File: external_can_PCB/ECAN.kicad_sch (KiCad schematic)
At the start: 32 parts, among them J1 JST GH 4, J3 JST GH 6, J4 Micro_SD_Card, J5 JST GH 6, U1 SN65HVD232, U2 AP2127N-3.3, U5 STM32L562RETx, Y1 8 Mhz

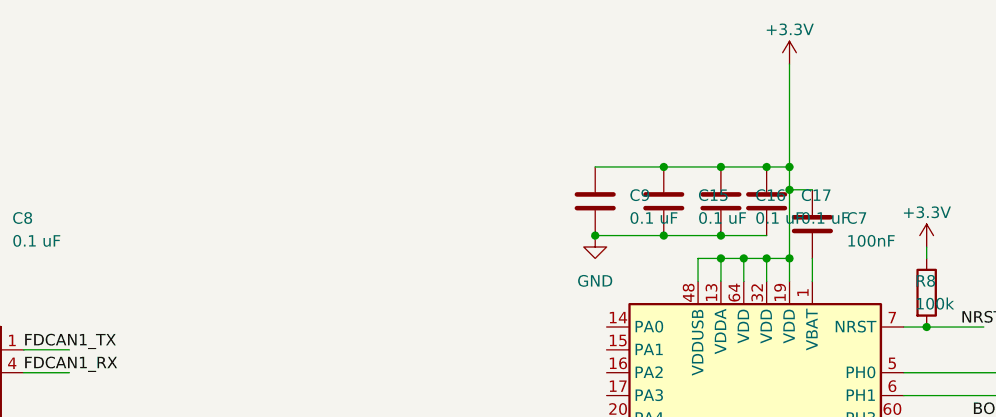
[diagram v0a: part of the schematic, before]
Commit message: Added screw holes and layer pours
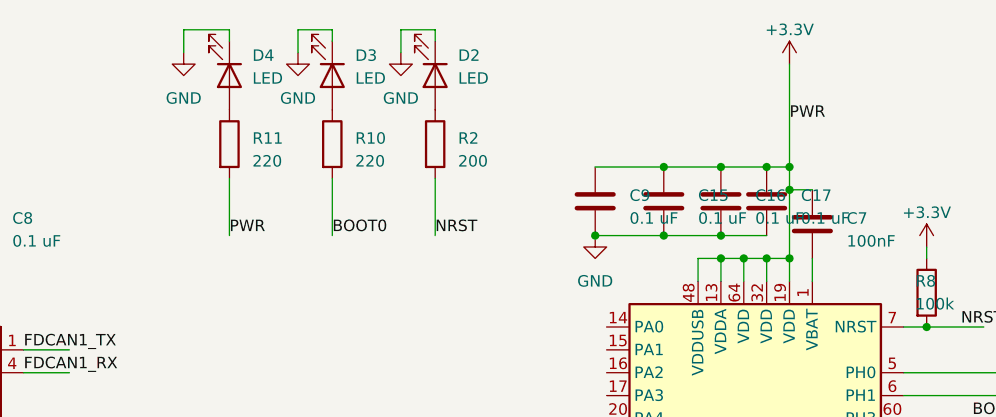
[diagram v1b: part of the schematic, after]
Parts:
- added D2, D3, D4: LED, LED_SMD:LED_0805_2012Metric_Pad1.15x1.40mm_HandSolder, symbol Device:LED
- added R10, R11: 220, Resistor_SMD:R_0402_1005Metric_Pad0.72x0.64mm_HandSolder, symbol Device:R
- added R2: 200, Resistor_SMD:R_0402_1005Metric_Pad0.72x0.64mm_HandSolder, symbol Device:R
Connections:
- net +3.3V: now also R11.2
- net BOOT0: now also R10.2
- net GND: now also D2.1 (K), D3.1 (K), D4.1 (K)
- net NRST: now also R2.2
- new net: D2.2 (A), R2.1
- new net: D4.2 (A), R11.1
- new net: D3.2 (A), R10.1

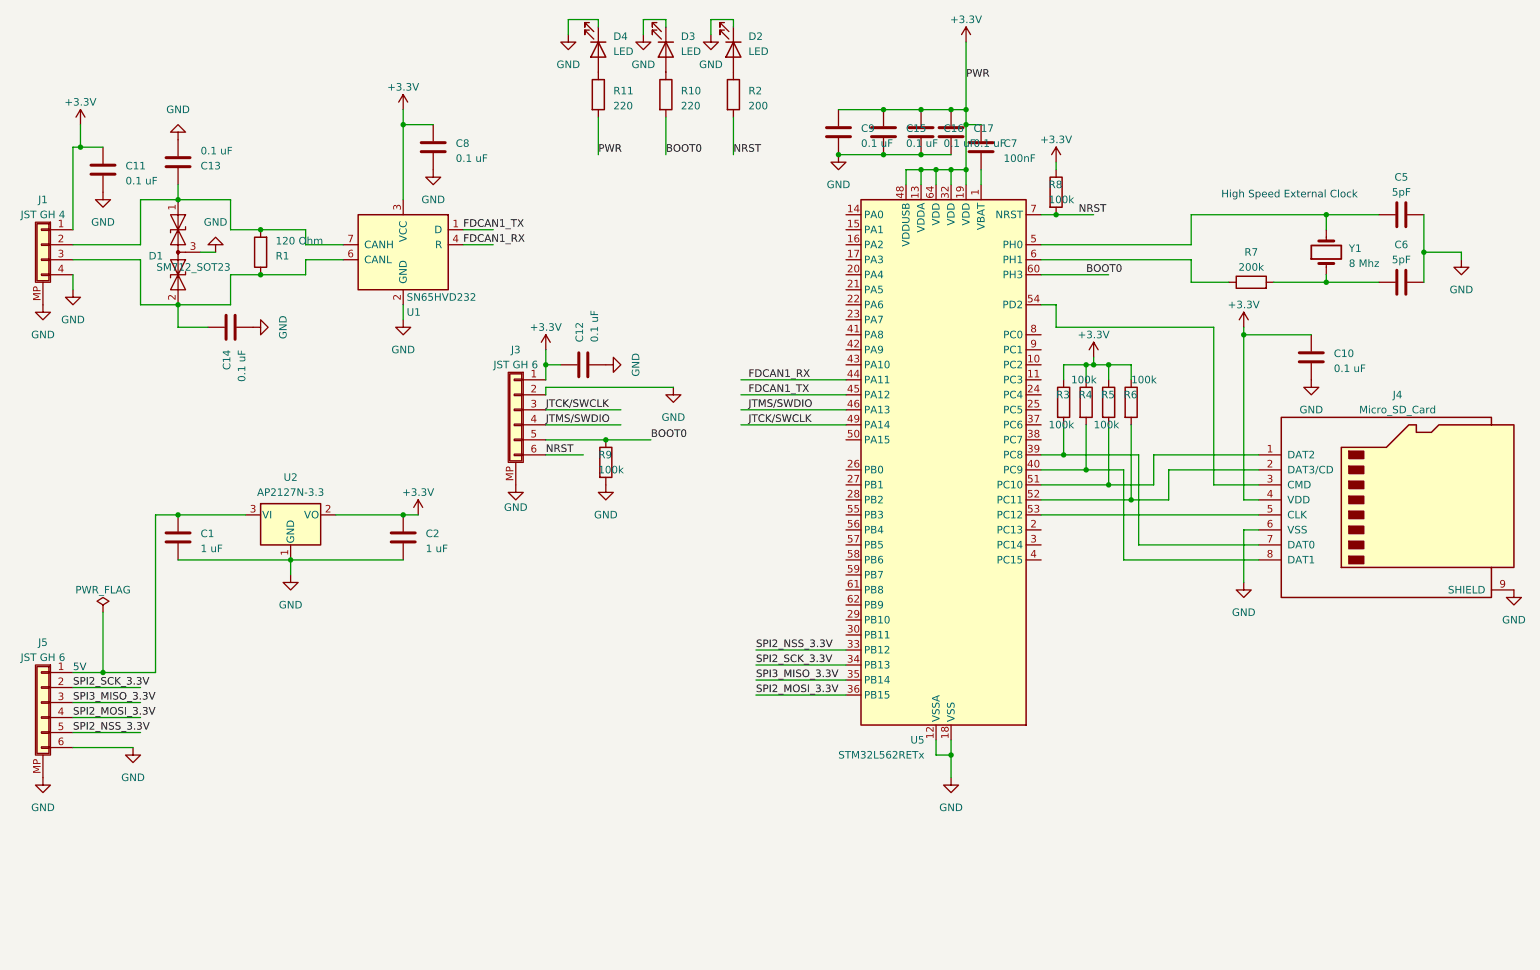
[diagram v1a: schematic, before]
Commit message: Addressed issues from Review by Olof
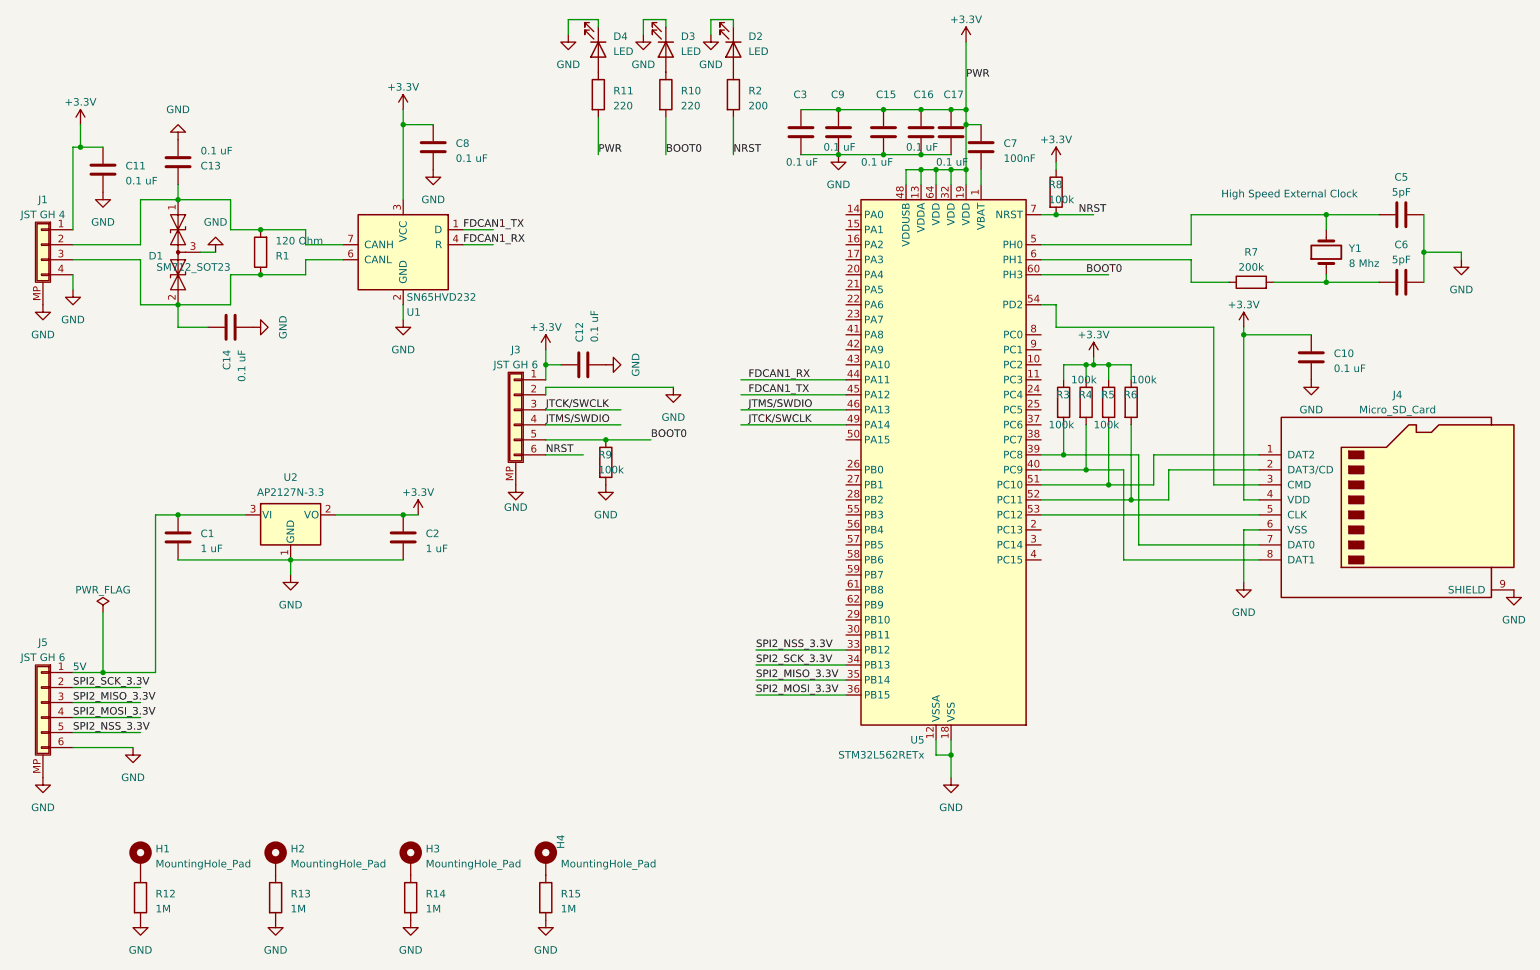
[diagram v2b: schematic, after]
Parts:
- added C3: 0.1 uF, Capacitor_SMD:C_0402_1005Metric_Pad0.74x0.62mm_HandSolder, symbol Device:C
- added H1, H2, H3, H4: MountingHole_Pad, MountingHole:MountingHole_3.2mm_M3_DIN965_Pad, symbol Mechanical:MountingHole_Pad
- added R12, R13, R14, R15: 1M, Resistor_SMD:R_0603_1608Metric_Pad0.98x0.95mm_HandSolder, symbol Device:R
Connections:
- net +3.3V: now also C3.1
- net GND: now also C3.2, R12.2, R13.2, R14.2, R15.2
- net SPI3_MISO_3.3V renamed SPI2_MISO_3.3V
- new net: H3.1, R14.1
- new net: H4.1, R15.1
- new net: H1.1, R12.1
- new net: H2.1, R13.1

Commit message: GPIO LED changes and UART connection to SPI lines
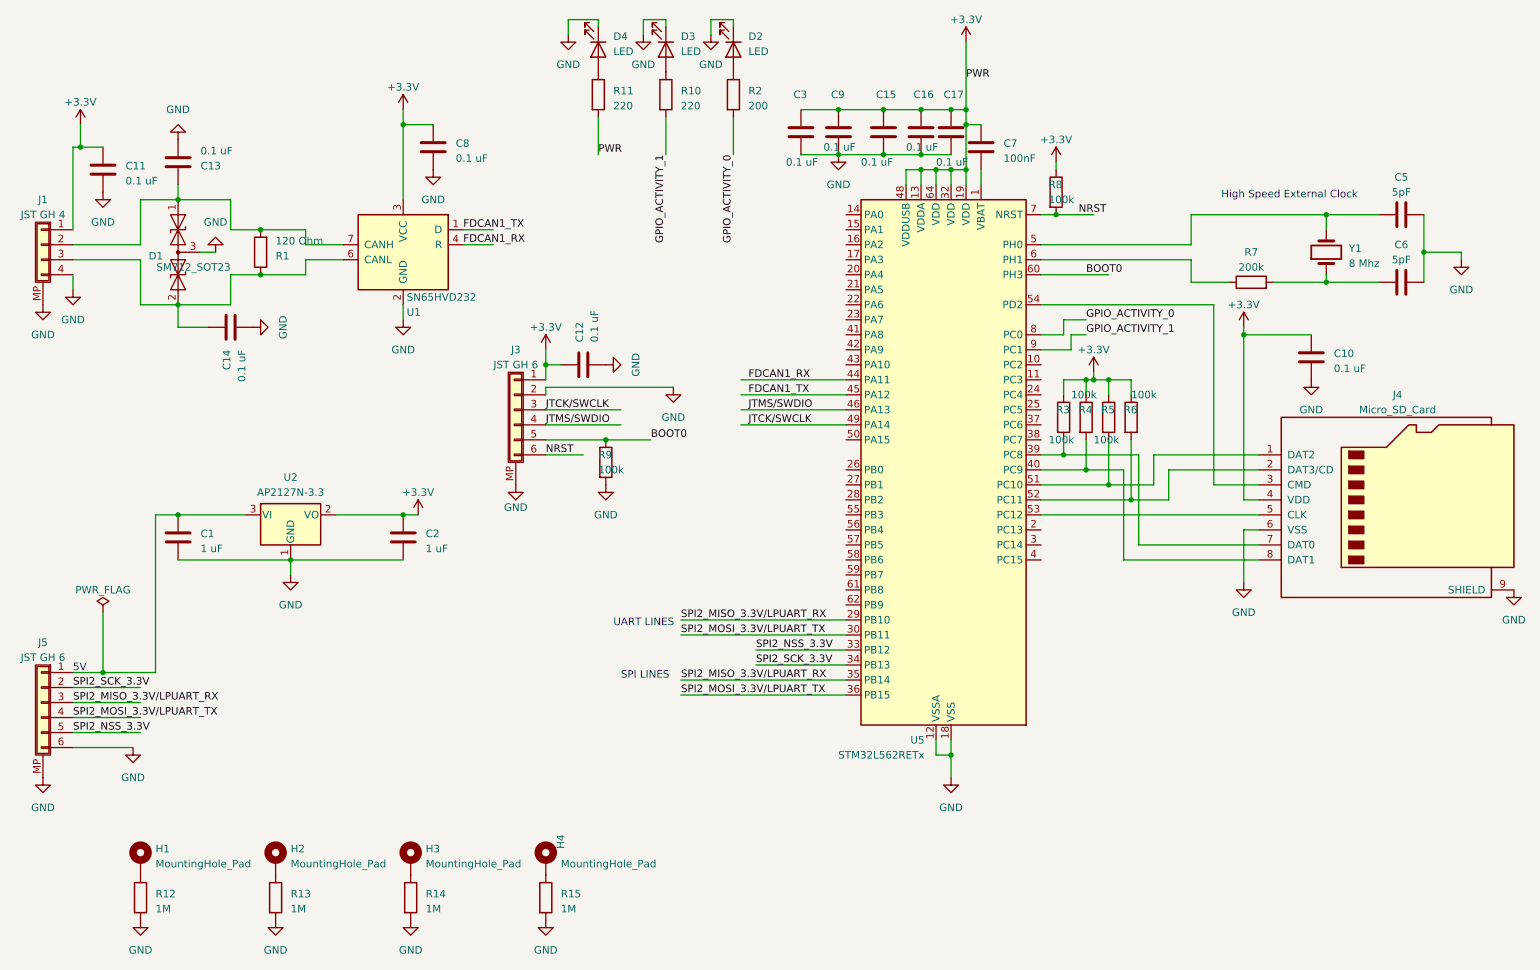
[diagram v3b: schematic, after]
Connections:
- net SPI2_MISO_3.3V is gone; now on net SPI2_MISO_3.3V/LPUART_RX: J5.3 (Pin_3), U5.35 (PB14)
- net SPI2_MOSI_3.3V is gone; now on net SPI2_MOSI_3.3V/LPUART_TX: J5.4 (Pin_4), U5.36 (PB15)
- net BOOT0: no longer R10.2
- net NRST: no longer R2.2
- net SPI2_MISO_3.3V/LPUART_RX: now reaches U5.29 (PB10)
- net SPI2_MOSI_3.3V/LPUART_TX: now reaches U5.30 (PB11)
- net GPIO_ACTIVITY_0: now reaches U5.8 (PC0)
- net GPIO_ACTIVITY_0: now also R2.2
- net GPIO_ACTIVITY_1: now reaches U5.9 (PC1)
- net GPIO_ACTIVITY_1: now also R10.2
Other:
- note added: "SPI LINES"
- note added: "UART LINES"
- moved on the sheet: R3, R4, R5, R6

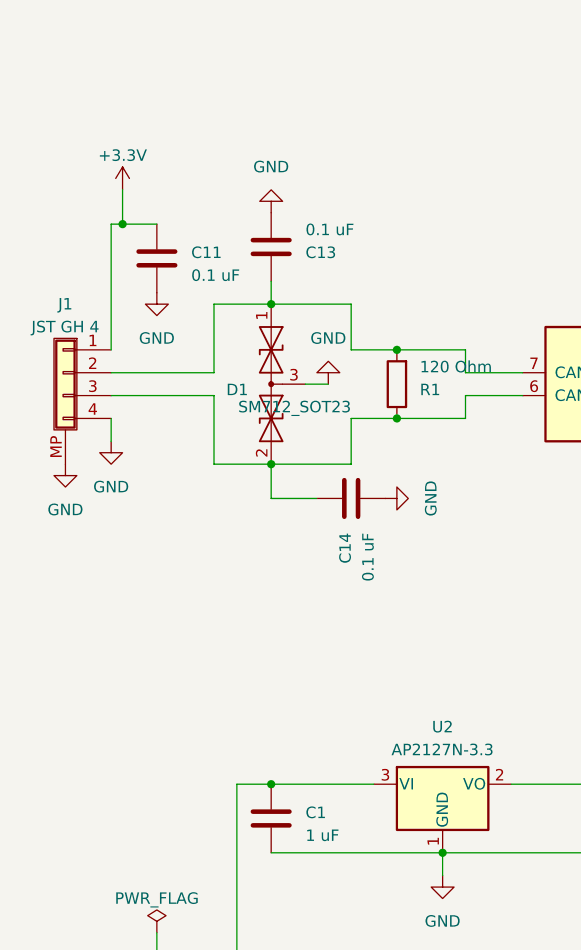
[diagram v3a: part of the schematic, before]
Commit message: Changed CAN connecter reference to 5V, which allows the board to be powered through the CAN connector
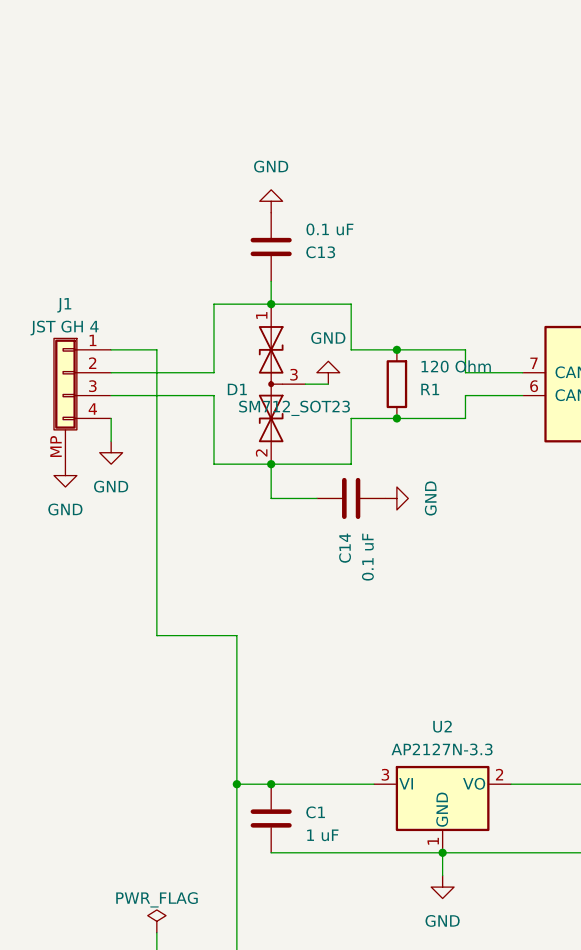
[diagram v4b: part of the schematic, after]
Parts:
- removed C11: 0.1 uF, Capacitor_SMD:C_0402_1005Metric_Pad0.74x0.62mm_HandSolder, symbol Device:C
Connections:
- net +3.3V: no longer J1.1 (Pin_1)
- net at C1.1, J5.1 (Pin_1), U2.3 (VI): now also J1.1 (Pin_1)
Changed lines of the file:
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@@
   (junction (at 83.82 99.06) (diameter 0) (color 0 0 0 0)
   )
-  (junction (at 29.21 36.83) (diameter 0) (color 0 0 0 0)
-  )
   (junction (at 165.1 30.48) (diameter 0) (color 0 0 0 0)
   )
@@
   (junction (at 157.48 38.1) (diameter 0) (color 0 0 0 0)
   )
+  (junction (at 41.91 99.06) (diameter 0) (color 0 0 0 0)
+  )
   (junction (at 59.69 50.8) (diameter 0) (color 0 0 0 0)
   )
@@
     (stroke (width 0) (type default))
   )
+  (wire (pts (xy 33.02 50.8) (xy 33.02 82.55))
+    (stroke (width 0) (type default))
+  )
   (wire (pts (xy 111.76 15.24) (xy 116.84 15.24))
     (stroke (width 0) (type default))
@@
     (stroke (width 0) (type default))
   )
-  (wire (pts (xy 27.94 36.83) (xy 29.21 36.83))
-    (stroke (width 0) (type default))
-  )
   (wire (pts (xy 158.75 116.84) (xy 130.81 116.84))
     (stroke (width 0) (type default))
@@
     (stroke (width 0) (type default))
   )
+  (wire (pts (xy 27.94 50.8) (xy 33.02 50.8))
+    (stroke (width 0) (type default))
+  )
   (wire (pts (xy 39.37 128.27) (xy 27.94 128.27))
     (stroke (width 0) (type default))
@@
     (stroke (width 0) (type default))
   )
-  (wire (pts (xy 33.02 36.83) (xy 29.21 36.83))
-    (stroke (width 0) (type default))
-  )
   (wire (pts (xy 195.58 78.74) (xy 195.58 76.2))
     (stroke (width 0) (type default))
@@
     (stroke (width 0) (type default))
   )
+  (wire (pts (xy 33.02 82.55) (xy 41.91 82.55))
+    (stroke (width 0) (type default))
+  )
   (wire (pts (xy 191.77 53.34) (xy 217.17 53.34))
     (stroke (width 0) (type default))
@@
     (stroke (width 0) (type default))
   )
-  (wire (pts (xy 27.94 50.8) (xy 27.94 36.83))
-    (stroke (width 0) (type default))
-  )
   (wire (pts (xy 195.58 66.04) (xy 199.39 66.04))
     (stroke (width 0) (type default))
@@
     (stroke (width 0) (type default))
   )
-  (wire (pts (xy 29.21 36.83) (xy 29.21 33.02))
+  (wire (pts (xy 41.91 82.55) (xy 41.91 99.06))
     (stroke (width 0) (type default))
   )
@@
         (path "/b319926f-f7f2-4b04-9478-39618a6f70ec"
           (reference "Y1") (unit 1)
-        )
-      )
-    )
-  )
-  (symbol (lib_id "Device:C") (at 33.02 40.64 0) (unit 1)
-    (in_bom yes) (on_board yes) (dnp no)
-    (property "Reference" "C11" (at 36.83 40.005 0)
-      (effects (font (size 1.27 1.27)) (justify left))
-    )
-    (property "Value" "0.1 uF" (at 36.83 42.545 0)
-      (effects (font (size 1.27 1.27)) (justify left))
-    )
-    (property "Footprint" "Capacitor_SMD:C_0402_1005Metric_Pad0.74x0.62mm_HandSolder" (at 33.9852 44.45 0)
-      (effects (font (size 1.27 1.27)) hide)
-    )
-    (property "Datasheet" "~" (at 33.02 40.64 0)
-      (effects (font (size 1.27 1.27)) hide)
-    )
-    (pin "1")
-    (pin "2")
-    (instances
-      (project "ECAN"
-        (path "/b319926f-f7f2-4b04-9478-39618a6f70ec"
-          (reference "C11") (unit 1)
         )
       )
@@
     )
   )
-  (symbol (lib_id "power:+3.3V") (at 29.21 33.02 0) (mirror y) (unit 1)
-    (in_bom yes) (on_board yes) (dnp no) (fields_autoplaced)
-    (property "Reference" "#PWR08" (at 29.21 36.83 0)
-      (effects (font (size 1.27 1.27)) hide)
-    )
-    (property "Value" "+3.3V" (at 29.21 29.21 0)
-      (effects (font (size 1.27 1.27)))
-    )
-    (property "Footprint" "" (at 29.21 33.02 0)
-      (effects (font (size 1.27 1.27)) hide)
-    )
-    (property "Datasheet" "" (at 29.21 33.02 0)
-      (effects (font (size 1.27 1.27)) hide)
-    )
-    (pin "1")
-    (instances
-      (project "ECAN"
-        (path "/b319926f-f7f2-4b04-9478-39618a6f70ec"
-          (reference "#PWR08") (unit 1)
-        )
-      )
-    )
-  )
   (symbol (lib_id "power:GND") (at 118.11 73.66 90) (mirror x) (unit 1)
     (in_bom yes) (on_board yes) (dnp no) (fields_autoplaced)
@@
         )
       )
-    )
-  )
-  (symbol (lib_id "power:GND") (at 33.02 44.45 0) (mirror y) (unit 1)
-    (in_bom yes) (on_board yes) (dnp no) (fields_autoplaced)
-    (property "Reference" "#PWR028" (at 33.02 50.8 0)
-      (effects (font (size 1.27 1.27)) hide)
-    )
-    (property "Value" "GND" (at 33.02 49.53 0)
-      (effects (font (size 1.27 1.27)))
-    )
-    (property "Footprint" "" (at 33.02 44.45 0)
-      (effects (font (size 1.27 1.27)) hide)
-    )
-    (property "Datasheet" "" (at 33.02 44.45 0)
-      (effects (font (size 1.27 1.27)) hide)
-    )
-    (pin "1")
-    (instances
-      (project "ECAN"
-        (path "/b319926f-f7f2-4b04-9478-39618a6f70ec"
-          (reference "#PWR028") (unit 1)
-        )
-      )
